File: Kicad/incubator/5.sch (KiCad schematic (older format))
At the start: 10 parts, among them U1 AP63205WU

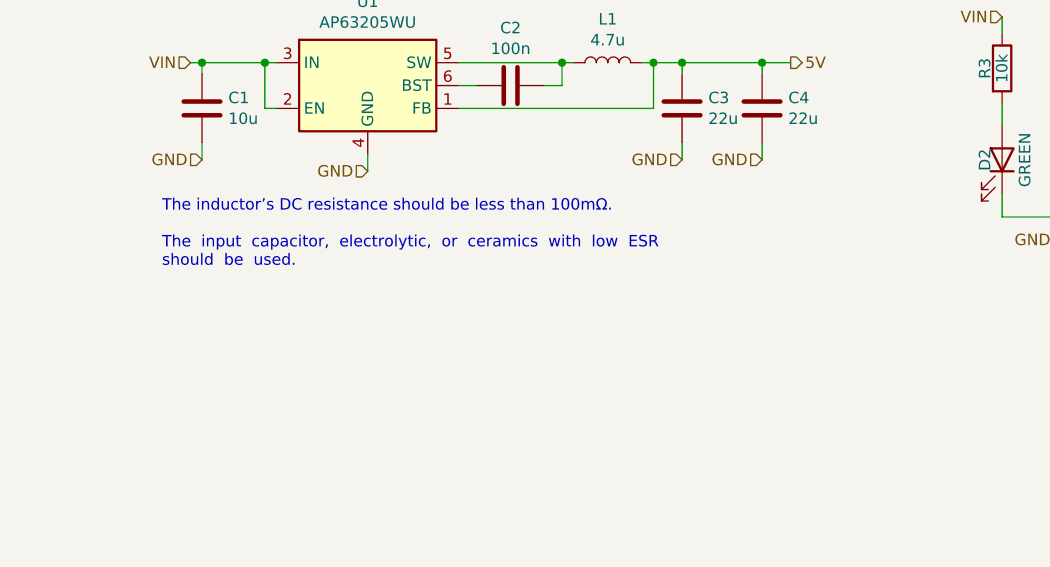
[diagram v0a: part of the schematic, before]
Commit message: fix: outline for incubator board
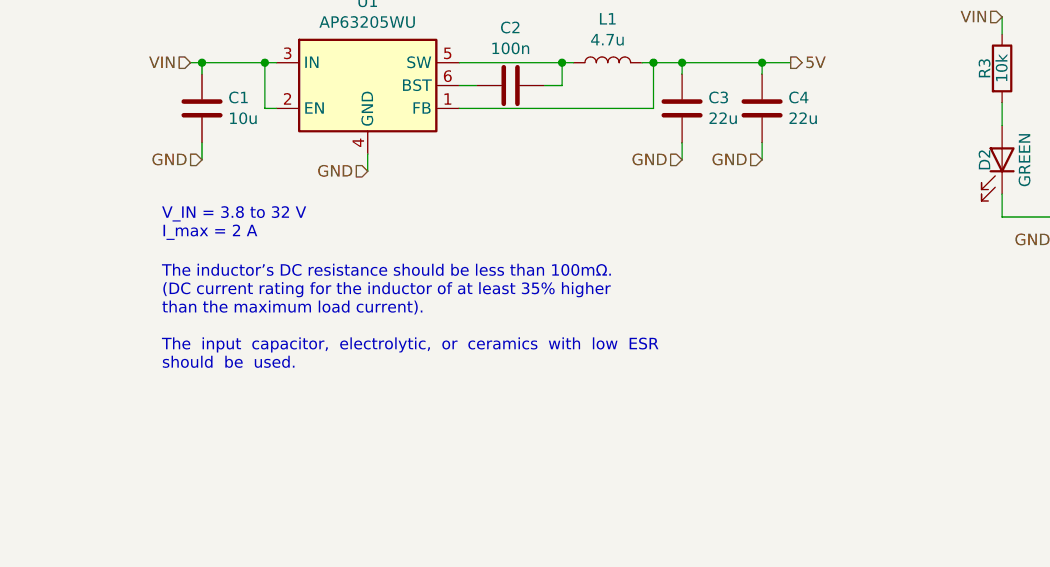
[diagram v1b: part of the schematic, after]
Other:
- note added: "The inductor’s DC resistance should be less than 100mΩ. \n(DC current rating for the inductor of at least 35% higher \nthan the maximum load current).\n \nThe input capacitor, electrolytic, or ceramics with low ESR\nshould be used."
- note added: "V_IN = 3.8 to 32 V\nI_max = 2 A"
- note removed: "The inductor’s DC resistance should be less than 100mΩ.\n \nThe input capacitor, electrolytic, or ceramics with low ESR\nshould be used."
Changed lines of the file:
@@
 Wire Wire Line
 	5800 4100 5800 4175
-Text Notes 3175 4650 0    50   ~ 0
-The inductor’s DC resistance should be less than 100mΩ.\n \nThe  input  capacitor,  electrolytic,  or  ceramics  with  low  ESR\nshould  be  used.
+Text Notes 3175 5100 0    50   ~ 0
+The inductor’s DC resistance should be less than 100mΩ. \n(DC current rating for the inductor of at least 35% higher \nthan the maximum load current).\n \nThe  input  capacitor,  electrolytic,  or  ceramics  with  low  ESR\nshould  be  used.
 Wire Wire Line
 	3350 3750 3625 3750
@@
 	1    0    0    -1
 $EndComp
+Text Notes 3175 4525 0    50   ~ 0
+V_IN = 3.8 to 32 V\nI_max = 2 A
 $EndSCHEMATC
